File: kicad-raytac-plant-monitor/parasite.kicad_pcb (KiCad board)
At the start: 4 copper layers, 49 x 126.4 mm, 55 parts, among them J1 TC2030-SWD, Q1 MMBT3906, Q4 Q_Photo_NPN, SW1 B3U-1000P, U1 nRF52840-QIAA, U2 SHTC3, Y1 32.768kHz, Y2 32MHz

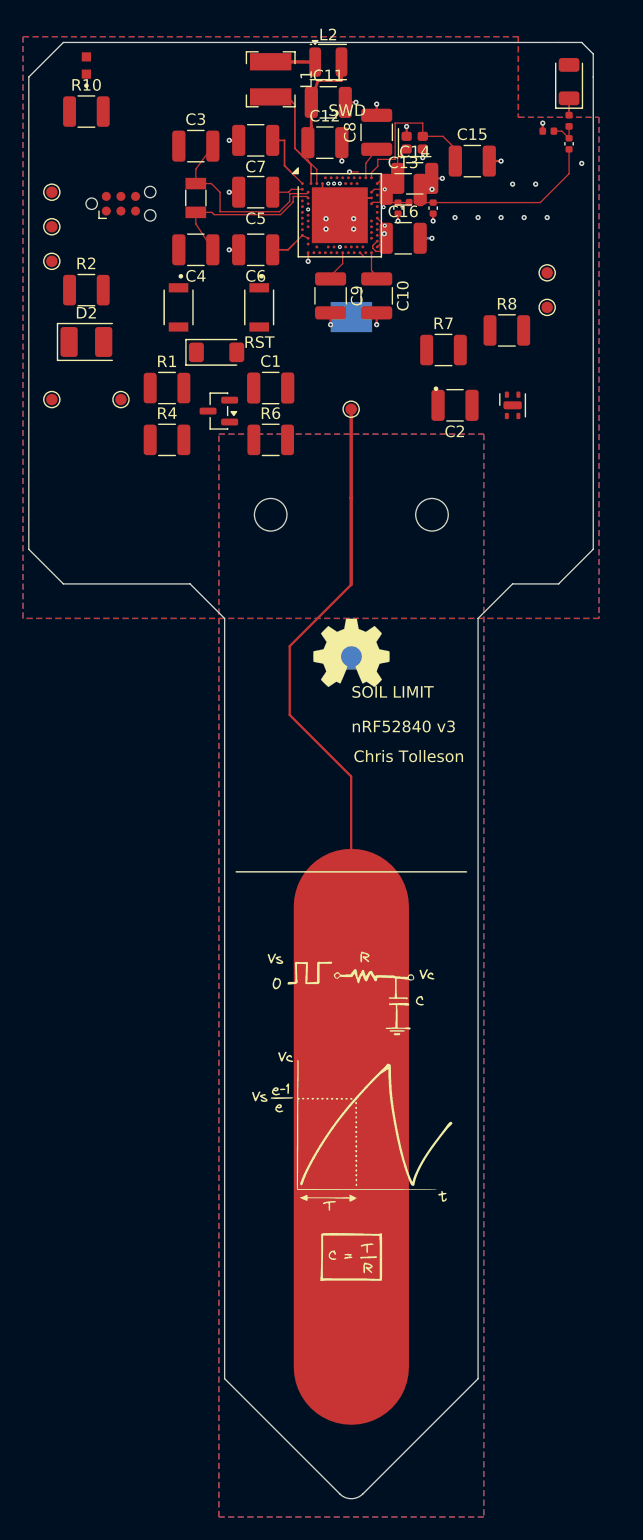
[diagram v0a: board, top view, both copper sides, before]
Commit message: feat: replace bare MCU with Raytac module and add debug I2C NFC interfaces
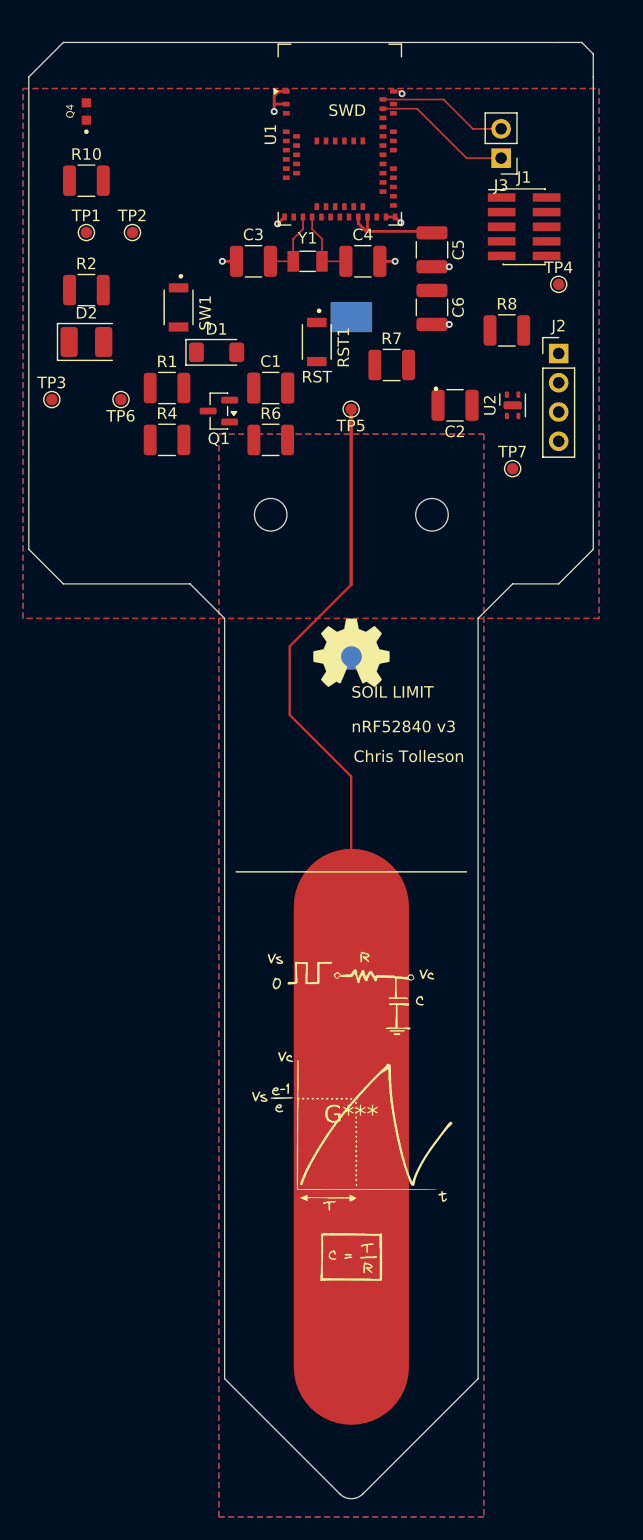
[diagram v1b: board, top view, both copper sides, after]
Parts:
- removed AE1: 2450AT18A0100001E, RF_Antenna:Johanson_2450AT18x100
- removed C10, C8, C9: 100n, Capacitor_SMD:C_1210_3225Metric
- removed C11, C7: 1u, Capacitor_SMD:C_1210_3225Metric
- removed C12: 47n, Capacitor_SMD:C_1210_3225Metric
- removed C13: 100p, Capacitor_SMD:C_1210_3225Metric
- removed C14, C15: 12p, Capacitor_SMD:C_1210_3225Metric
- removed C16: 820p, Capacitor_SMD:C_1210_3225Metric
- removed C17: 0.8p, Capacitor_SMD:C_0402_1005Metric
- removed C18: 0.5p, Capacitor_SMD:C_0402_1005Metric
- removed C19: 1p, Capacitor_SMD:C_0402_1005Metric
- removed L1: 10u, Inductor_SMD:L_Bourns-SRN4018
- removed L2: 15n, Inductor_SMD:L_Coilcraft_1008HQ_2520Metric
- removed L3: 4.7n, Inductor_SMD:L_0402_1005Metric
- removed L4: 2.7n, Inductor_SMD:L_0402_1005Metric
- removed L5: 3.9n, Inductor_SMD:L_0402_1005Metric
- removed TP8: 0.10, TestPoint:TestPoint_Pad_D1.0mm
- removed Y2: 32MHz, Crystal:Crystal_SMD_2016-4Pin_2.0x1.6mm
- added J2: I2C 3V, Connector_PinHeader_2.54mm:PinHeader_1x04_P2.54mm_Vertical, F.Cu at (86.0, 54.0)
- added J3: NFC ANTENNA, Connector_PinHeader_2.54mm:PinHeader_1x02_P2.54mm_Vertical, F.Cu at (81.0, 37.0)
- C6: value 4.7u -> 10u
- J1: value TC2030-SWD -> Cortex SWD 10-pin; footprint Connector:Tag-Connect_TC2030-IDC-NL_2x03_P1.27mm_Vertical -> Connector_PinHeader_1.27mm:PinHeader_2x05_P1.27mm_Vertical_SMD
- U1: value nRF52840-QIAA -> MDBT50Q-1MV2; footprint Package_DFN_QFN:Nordic_AQFN-73-1EP_7x7mm_P0.5mm -> RF_Module:Raytac_MDBT50Q
- moved J1 35.1 mm to (83.0, 43.0)
- moved C5 16.1 mm to (75.0, 45.0), turned to -90 degrees
- moved C6 16.1 mm to (75.0, 50.0), turned to -90 degrees
- moved C4 14.5 mm to (69.0, 46.0), turned to 0 degrees
- moved TP7 14.3 mm to (82.0, 64.0)
- moved TP3 12.0 mm to (42.0, 58.0)
- moved C3 11.2 mm to (59.5, 46.0)
- moved Y1 11.2 mm to (64.2, 46.0), turned to 0 degrees
- moved TP2 7.02 mm to (49.0, 43.5)
- moved U1 7.00 mm to (67.0, 35.0)
- moved R10 6.00 mm to (45.0, 39.0)
- moved RST1 5.83 mm to (65.0, 53.0)
- moved R7 4.68 mm to (71.5, 55.0)
- moved TP1 4.61 mm to (45.0, 43.5)
- moved Q4 4.00 mm to (45.0, 33.0)
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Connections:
- C5 pad 1: DEC1 -> +3V0
- J1 pad 3: RST -> GND
- J1 pad 6: unconnected-(J1-Pin_6-Pad6) -> SWO
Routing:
- net RF_50: track 16.1 -> 0.00 mm
- net XC2: track 14.4 -> 0.00 mm
- net DEC4_6: track 13.1 -> 0.00 mm
- net NFC1: track 0.00 -> 12.0 mm
- net NFC2: track 0.00 -> 11.3 mm
- net XL1: track 16.6 -> 6.18 mm
- net SWDIO: track 10.4 -> 0.00 mm, vias 1 -> 0
- net DCC: track 9.81 -> 0.00 mm
- net +3V0: track 18.1 -> 8.54 mm, vias 1 -> 0
- net XL2: track 14.5 -> 6.28 mm
- net GND: track 17.6 -> 12.4 mm, vias 31 -> 8
- net XC1: track 4.88 -> 0.00 mm
- net Net-(L1-Pad2): track 3.86 -> 0.00 mm
- net RST: track 3.39 -> 0.00 mm, vias 1 -> 0
- net RF_SOC: track 3.33 -> 0.00 mm
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
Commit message: feat: route Raytac module and debug interfaces with standard through vias
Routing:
- net +3V0: track 8.54 -> 72.6 mm, vias 0 -> 1
- net SWDIO: track 0.00 -> 52.7 mm, vias 0 -> 3
- net SWDCLK: track 0.00 -> 52.1 mm, vias 0 -> 3
- net SDA: track 0.00 -> 48.8 mm, vias 0 -> 2
- net SCL: track 0.00 -> 47.7 mm, vias 0 -> 1
- net RST: track 0.00 -> 41.9 mm, vias 0 -> 2
- net SENS_OUT: track 0.00 -> 35.0 mm, vias 0 -> 2
- net PWM: track 0.00 -> 33.3 mm, vias 0 -> 2
- net SWO: track 0.00 -> 30.7 mm, vias 0 -> 2
- net PHOTO_OUT: track 0.00 -> 27.7 mm, vias 0 -> 2
- net CPARA: track 87.6 -> 112.9 mm
- net LED: track 0.00 -> 24.4 mm, vias 0 -> 2
- net PHOTO_V: track 0.00 -> 23.6 mm, vias 0 -> 2
- net BTN1: track 0.00 -> 16.4 mm, vias 0 -> 2
- net Net-(Q1-B): track 0.00 -> 11.4 mm, vias 0 -> 2
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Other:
- board text added: "D2"
- board text added: "I2C"
- board text added: "J3 NFC"
- board text added: "MODULE-A"
- board text added: "SW1"
- board text removed: "nRF52840 v3"

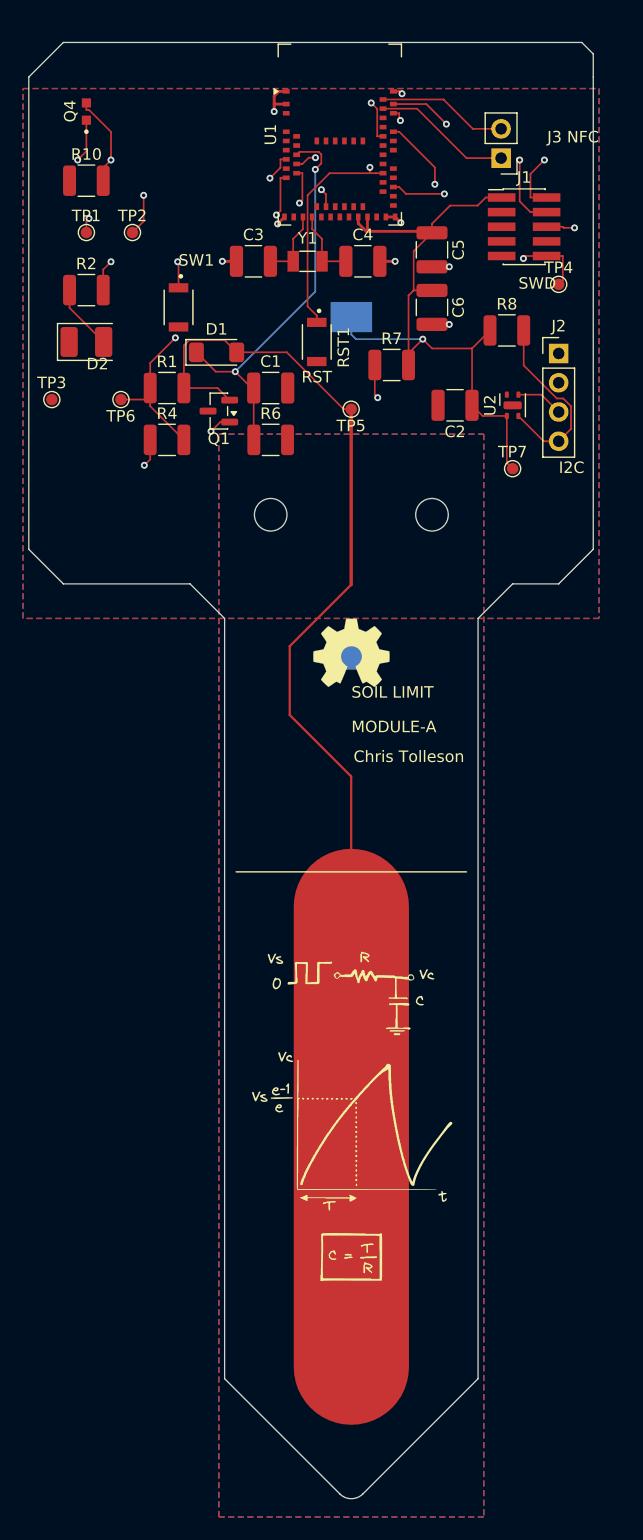
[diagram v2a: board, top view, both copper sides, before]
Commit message: feat: compact Raytac monitor with 0805 passives and straight 30 mm sides
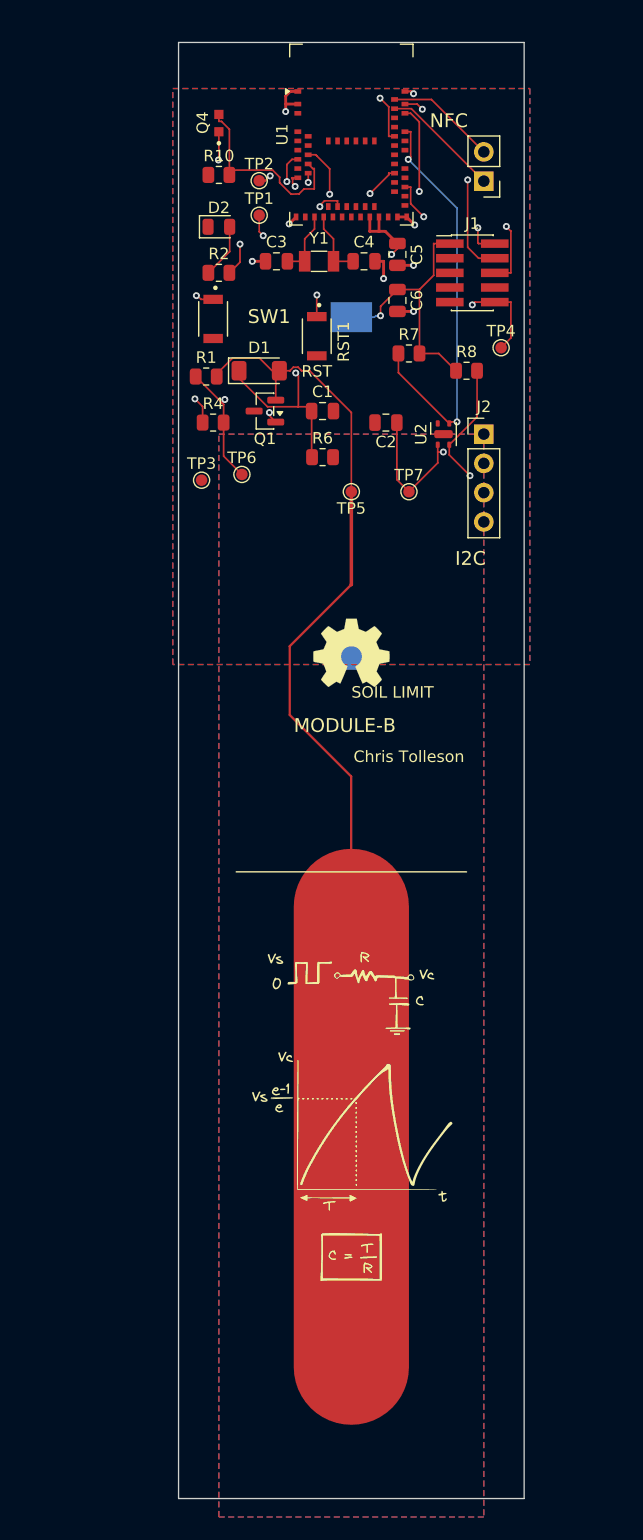
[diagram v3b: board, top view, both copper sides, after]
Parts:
- C1, C2, C3, C4, C5, C6: footprint Capacitor_SMD:C_1210_3225Metric -> Capacitor_SMD:C_0805_2012Metric
- D2: footprint LED_SMD:LED_PLCC-2_3.4x3.0mm_KA -> LED_SMD:LED_0805_2012Metric
- R1, R10, R2, R4, R6, R7, R8: footprint Resistor_SMD:R_1210_3225Metric -> Resistor_SMD:R_0805_2012Metric
- moved D2 15.2 mm to (56.5, 43.0)
- moved TP1 15.1 mm to (60.0, 42.0)
- moved TP3 14.8 mm to (55.0, 65.0)
- moved TP6 12.3 mm to (58.5, 64.5), turned to 0 degrees
- moved TP2 11.9 mm to (60.0, 39.0)
- moved R2 11.6 mm to (56.5, 47.0)
- moved Q4 11.5 mm to (56.5, 34.0)
- moved R10 11.5 mm to (56.5, 38.5)
- moved J2 9.55 mm to (79.5, 61.0)
- moved TP7 9.22 mm to (73.0, 66.0)
- moved TP4 7.43 mm to (81.0, 53.5)
- moved TP5 7.16 mm to (68.0, 66.0)
- moved U2 6.50 mm to (76.0, 61.0)
- moved C2 6.18 mm to (71.0, 60.0)
- moved J1 6.02 mm to (78.5, 47.0)
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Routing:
- net SWDIO: track 52.7 -> 34.1 mm
- net SWDCLK: track 52.1 -> 34.8 mm
- net LED: track 24.4 -> 11.8 mm
- net PHOTO_V: track 23.6 -> 11.9 mm
- net PHOTO_OUT: track 27.7 -> 16.9 mm, vias 2 -> 0
- net CPARA: track 112.9 -> 104.5 mm
- net +3V0: track 72.6 -> 65.8 mm, vias 1 -> 3
- net RST: track 41.9 -> 35.8 mm, vias 2 -> 3
- net SDA: track 48.8 -> 43.5 mm
- net SWO: track 30.7 -> 28.9 mm
- net NFC2: track 11.3 -> 9.63 mm
- net NFC1: track 12.0 -> 10.4 mm
- net SCL: track 47.7 -> 46.1 mm, vias 1 -> 2
- net SENS_OUT: track 35.0 -> 36.5 mm
- net GND: track 12.4 -> 13.6 mm
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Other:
- board size 49 x 126.4 mm -> 30 x 126.4 mm
- board text added: "MODULE-B"
- board text added: "NFC"
- board text removed: "D2"
- board text removed: "J3 NFC"
- board text removed: "MODULE-A"
- board text removed: "SWD"
